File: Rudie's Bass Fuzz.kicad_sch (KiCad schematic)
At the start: 15 parts, among them J1 Conn_01x01_Male, J2 Conn_01x01_Male, J3 Conn_01x01_Male, J4 Conn_01x01_Male, Q1 BC549

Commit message: added led to pcb design
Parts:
- D2: footprint (none) -> LED_THT:LED_D5.0mm
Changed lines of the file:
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@@
     (property "Reference" "D2" (id 0) (at 89.8525 43.18 0))
     (property "Value" "LED" (id 1) (at 89.8525 45.72 0))
-    (property "Footprint" "" (id 2) (at 88.265 50.165 0)
+    (property "Footprint" "LED_THT:LED_D5.0mm" (id 2) (at 88.265 50.165 0)
       (effects (font (size 1.27 1.27)) hide)
     )
@@
     )
     (path "/9bac20ab-0eff-4b4e-96fd-8a8eb787d966"
-      (reference "D2") (unit 1) (value "LED") (footprint "")
+      (reference "D2") (unit 1) (value "LED") (footprint "LED_THT:LED_D5.0mm")
     )
     (path "/0309e1ab-0658-4dbf-89ab-e051ee8674ac"

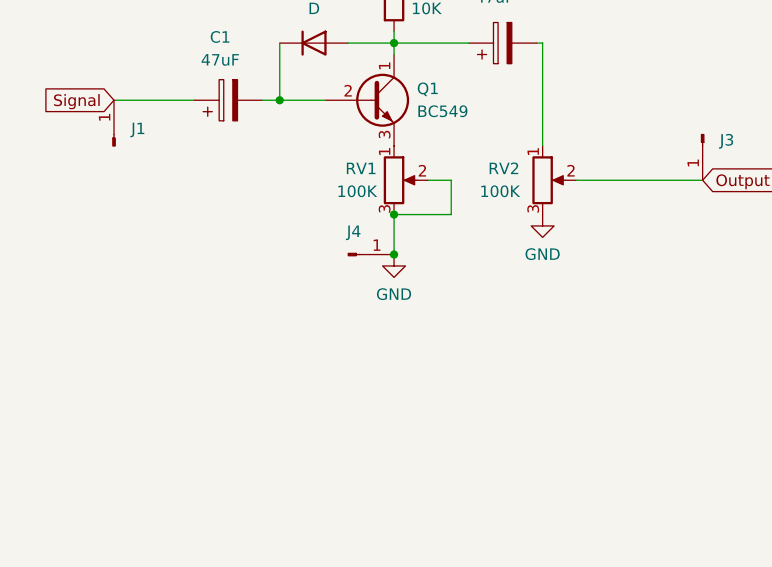
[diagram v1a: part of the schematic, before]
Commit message: removed wires and added extra gnd pins
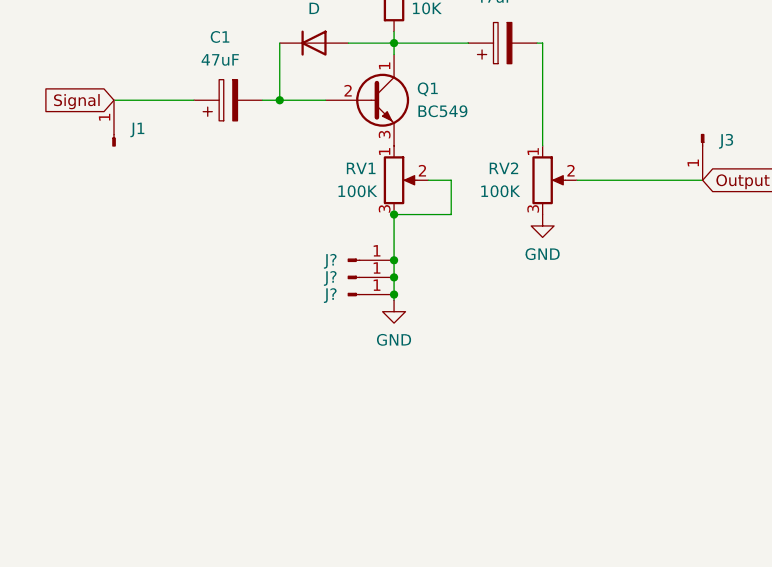
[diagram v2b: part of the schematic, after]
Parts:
- removed J4: Conn_01x01_Male, Connector_Pin:Pin_D1.4mm_L8.5mm_W2.8mm_FlatFork, symbol Connector:Conn_01x01_Male
- added J? (x3): Conn_01x01_Male, Connector_Pin:Pin_D1.4mm_L8.5mm_W2.8mm_FlatFork, symbol Connector:Conn_01x01_Male
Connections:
- net GND: now also J?.1 (Pin_1), J?.1 (Pin_1), J?.1 (Pin_1)
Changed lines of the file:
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@@
   (junction (at 107.315 83.82) (diameter 0) (color 0 0 0 0)
   )
-  (junction (at 107.315 88.265) (diameter 0) (color 0 0 0 0)
-  )
   (junction (at 94.615 71.12) (diameter 0) (color 0 0 0 0)
   )
+  (junction (at 107.315 90.805) (diameter 0) (color 0 0 0 0)
+  )
+  (junction (at 107.315 92.71) (diameter 0) (color 0 0 0 0)
+  )
+  (junction (at 107.315 88.9) (diameter 0) (color 0 0 0 0)
+  )
   (junction (at 84.455 40.64) (diameter 0) (color 0 0 0 0)
   )
@@
     (stroke (width 0) (type default) (color 0 0 0 0))
   )
+  (wire (pts (xy 107.315 88.9) (xy 107.315 90.805))
+    (stroke (width 0) (type default) (color 0 0 0 0))
+  )
+  (wire (pts (xy 107.315 92.71) (xy 107.315 93.345))
+    (stroke (width 0) (type default) (color 0 0 0 0))
+  )
   (wire (pts (xy 84.455 40.64) (xy 107.315 40.64))
     (stroke (width 0) (type default) (color 0 0 0 0))
@@
     (stroke (width 0) (type default) (color 0 0 0 0))
   )
-  (wire (pts (xy 107.315 88.265) (xy 107.315 83.82))
-    (stroke (width 0) (type default) (color 0 0 0 0))
-  )
   (wire (pts (xy 107.315 64.77) (xy 107.315 66.04))
     (stroke (width 0) (type default) (color 0 0 0 0))
@@
     (stroke (width 0) (type default) (color 0 0 0 0))
   )
+  (wire (pts (xy 107.315 83.82) (xy 107.315 88.9))
+    (stroke (width 0) (type default) (color 0 0 0 0))
+  )
   (wire (pts (xy 84.455 40.64) (xy 84.455 50.165))
     (stroke (width 0) (type default) (color 0 0 0 0))
@@
   )
   (wire (pts (xy 127.635 80.01) (xy 141.605 80.01))
+    (stroke (width 0) (type default) (color 0 0 0 0))
+  )
+  (wire (pts (xy 107.315 90.805) (xy 107.315 92.71))
     (stroke (width 0) (type default) (color 0 0 0 0))
   )
@@
     (pin "1")
   )
-  (symbol (lib_id "power:GND") (at 107.315 88.265 0) (unit 1)
-    (in_bom yes) (on_board yes) (fields_autoplaced)
-    (property "Reference" "#PWR01" (id 0) (at 107.315 94.615 0)
-      (effects (font (size 1.27 1.27)) hide)
-    )
-    (property "Value" "GND" (id 1) (at 107.315 92.71 0))
-    (property "Footprint" "" (id 2) (at 107.315 88.265 0)
-      (effects (font (size 1.27 1.27)) hide)
-    )
-    (property "Datasheet" "" (id 3) (at 107.315 88.265 0)
+  (symbol (lib_id "power:GND") (at 107.315 93.345 0) (unit 1)
+    (in_bom yes) (on_board yes) (fields_autoplaced)
+    (property "Reference" "#PWR01" (id 0) (at 107.315 99.695 0)
+      (effects (font (size 1.27 1.27)) hide)
+    )
+    (property "Value" "GND" (id 1) (at 107.315 97.79 0))
+    (property "Footprint" "" (id 2) (at 107.315 93.345 0)
+      (effects (font (size 1.27 1.27)) hide)
+    )
+    (property "Datasheet" "" (id 3) (at 107.315 93.345 0)
       (effects (font (size 1.27 1.27)) hide)
     )
@@
     )
     (property "Datasheet" "~" (id 3) (at 141.605 74.93 0)
-      (effects (font (size 1.27 1.27)) hide)
-    )
-    (pin "1")
-  )
-  (symbol (lib_id "Connector:Conn_01x01_Male") (at 102.235 88.265 0) (unit 1)
-    (in_bom yes) (on_board yes) (fields_autoplaced)
-    (property "Reference" "J4" (id 0) (at 102.87 85.725 0))
-    (property "Value" "Conn_01x01_Male" (id 1) (at 104.1399 86.995 90)
-      (effects (font (size 1.27 1.27)) (justify left) hide)
-    )
-    (property "Footprint" "Connector_Pin:Pin_D1.4mm_L8.5mm_W2.8mm_FlatFork" (id 2) (at 102.235 88.265 0)
-      (effects (font (size 1.27 1.27)) hide)
-    )
-    (property "Datasheet" "~" (id 3) (at 102.235 88.265 0)
       (effects (font (size 1.27 1.27)) hide)
     )
@@
     (pin "2")
   )
+  (symbol (lib_id "Connector:Conn_01x01_Male") (at 102.235 92.71 0) (unit 1)
+    (in_bom yes) (on_board yes)
+    (property "Reference" "J?" (id 0) (at 100.33 92.71 0))
+    (property "Value" "Conn_01x01_Male" (id 1) (at 104.1399 91.44 90)
+      (effects (font (size 1.27 1.27)) (justify left) hide)
+    )
+    (property "Footprint" "Connector_Pin:Pin_D1.4mm_L8.5mm_W2.8mm_FlatFork" (id 2) (at 102.235 92.71 0)
+      (effects (font (size 1.27 1.27)) hide)
+    )
+    (property "Datasheet" "~" (id 3) (at 102.235 92.71 0)
+      (effects (font (size 1.27 1.27)) hide)
+    )
+    (pin "1")
+  )
   (symbol (lib_id "Device:C_Polarized") (at 88.9 71.12 90) (unit 1)
     (in_bom yes) (on_board yes)
@@
     (pin "1")
   )
+  (symbol (lib_id "Connector:Conn_01x01_Male") (at 102.235 90.805 0) (unit 1)
+    (in_bom yes) (on_board yes)
+    (property "Reference" "J?" (id 0) (at 100.33 90.805 0))
+    (property "Value" "Conn_01x01_Male" (id 1) (at 104.1399 89.535 90)
+      (effects (font (size 1.27 1.27)) (justify left) hide)
+    )
+    (property "Footprint" "Connector_Pin:Pin_D1.4mm_L8.5mm_W2.8mm_FlatFork" (id 2) (at 102.235 90.805 0)
+      (effects (font (size 1.27 1.27)) hide)
+    )
+    (property "Datasheet" "~" (id 3) (at 102.235 90.805 0)
+      (effects (font (size 1.27 1.27)) hide)
+    )
+    (pin "1")
+  )
+  (symbol (lib_id "Connector:Conn_01x01_Male") (at 102.235 88.9 0) (unit 1)
+    (in_bom yes) (on_board yes)
+    (property "Reference" "J?" (id 0) (at 100.33 88.9 0))
+    (property "Value" "Conn_01x01_Male" (id 1) (at 104.1399 87.63 90)
+      (effects (font (size 1.27 1.27)) (justify left) hide)
+    )
+    (property "Footprint" "Connector_Pin:Pin_D1.4mm_L8.5mm_W2.8mm_FlatFork" (id 2) (at 102.235 88.9 0)
+      (effects (font (size 1.27 1.27)) hide)
+    )
+    (property "Datasheet" "~" (id 3) (at 102.235 88.9 0)
+      (effects (font (size 1.27 1.27)) hide)
+    )
+    (pin "1")
+  )
   (sheet_instances
     (path "/" (page "1"))
@@
       (reference "J3") (unit 1) (value "Conn_01x01_Male") (footprint "Connector_Pin:Pin_D1.4mm_L8.5mm_W2.8mm_FlatFork")
     )
-    (path "/7a1a31a1-be13-4299-817f-015138e93643"
-      (reference "J4") (unit 1) (value "Conn_01x01_Male") (footprint "Connector_Pin:Pin_D1.4mm_L8.5mm_W2.8mm_FlatFork")
+    (path "/84696f8a-20a3-40b7-aedb-09285a52328e"
+      (reference "J?") (unit 1) (value "Conn_01x01_Male") (footprint "Connector_Pin:Pin_D1.4mm_L8.5mm_W2.8mm_FlatFork")
+    )
+    (path "/e27eb912-b00a-4827-9110-e3585acda442"
+      (reference "J?") (unit 1) (value "Conn_01x01_Male") (footprint "Connector_Pin:Pin_D1.4mm_L8.5mm_W2.8mm_FlatFork")
+    )
+    (path "/ed80c364-dffb-4bce-83fe-922f0e755acb"
+      (reference "J?") (unit 1) (value "Conn_01x01_Male") (footprint "Connector_Pin:Pin_D1.4mm_L8.5mm_W2.8mm_FlatFork")
     )
     (path "/ac98c4da-cede-4def-8a6f-fc1401ef6f5d"

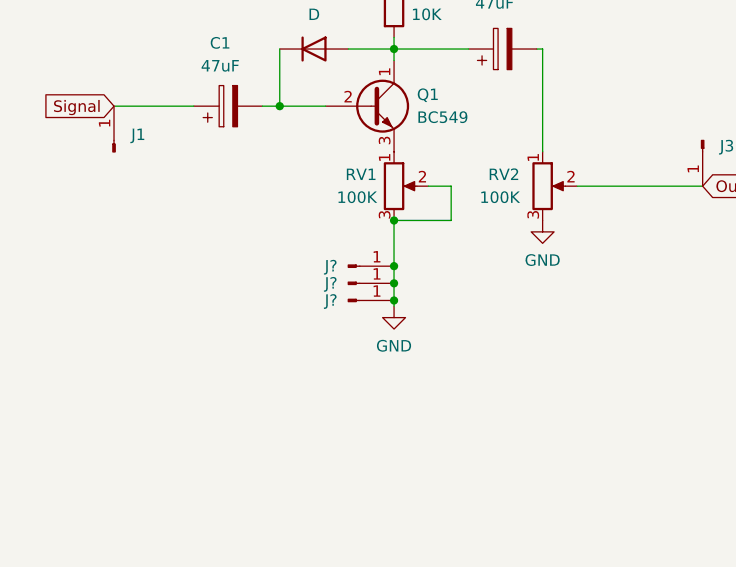
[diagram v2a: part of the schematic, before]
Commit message: silkscreen cleanup
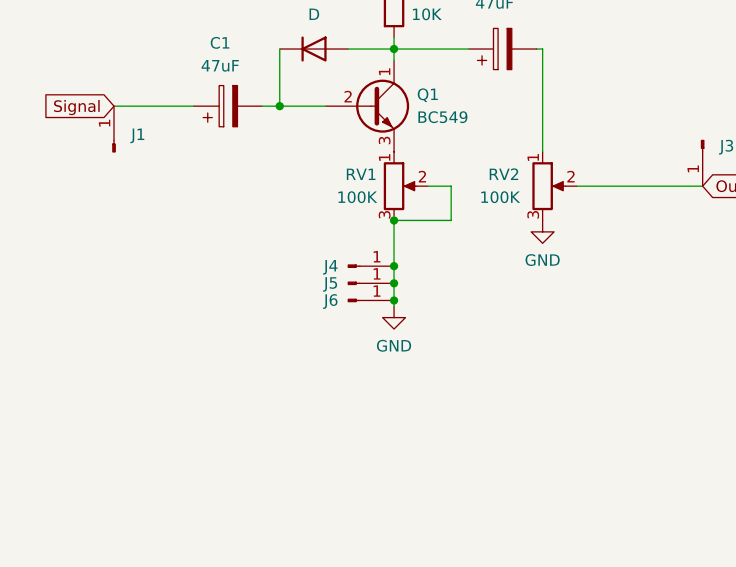
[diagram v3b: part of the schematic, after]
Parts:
- gave numbers to parts that had none: 3
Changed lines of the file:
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@@
   (symbol (lib_id "Connector:Conn_01x01_Male") (at 102.235 92.71 0) (unit 1)
     (in_bom yes) (on_board yes)
-    (property "Reference" "J?" (id 0) (at 100.33 92.71 0))
+    (property "Reference" "J6" (id 0) (at 100.33 92.71 0))
     (property "Value" "Conn_01x01_Male" (id 1) (at 104.1399 91.44 90)
       (effects (font (size 1.27 1.27)) (justify left) hide)
@@
   (symbol (lib_id "Connector:Conn_01x01_Male") (at 102.235 90.805 0) (unit 1)
     (in_bom yes) (on_board yes)
-    (property "Reference" "J?" (id 0) (at 100.33 90.805 0))
+    (property "Reference" "J5" (id 0) (at 100.33 90.805 0))
     (property "Value" "Conn_01x01_Male" (id 1) (at 104.1399 89.535 90)
       (effects (font (size 1.27 1.27)) (justify left) hide)
@@
   (symbol (lib_id "Connector:Conn_01x01_Male") (at 102.235 88.9 0) (unit 1)
     (in_bom yes) (on_board yes)
-    (property "Reference" "J?" (id 0) (at 100.33 88.9 0))
+    (property "Reference" "J4" (id 0) (at 100.33 88.9 0))
     (property "Value" "Conn_01x01_Male" (id 1) (at 104.1399 87.63 90)
       (effects (font (size 1.27 1.27)) (justify left) hide)
@@
       (reference "J3") (unit 1) (value "Conn_01x01_Male") (footprint "Connector_Pin:Pin_D1.4mm_L8.5mm_W2.8mm_FlatFork")
     )
+    (path "/ed80c364-dffb-4bce-83fe-922f0e755acb"
+      (reference "J4") (unit 1) (value "Conn_01x01_Male") (footprint "Connector_Pin:Pin_D1.4mm_L8.5mm_W2.8mm_FlatFork")
+    )
+    (path "/e27eb912-b00a-4827-9110-e3585acda442"
+      (reference "J5") (unit 1) (value "Conn_01x01_Male") (footprint "Connector_Pin:Pin_D1.4mm_L8.5mm_W2.8mm_FlatFork")
+    )
     (path "/84696f8a-20a3-40b7-aedb-09285a52328e"
-      (reference "J?") (unit 1) (value "Conn_01x01_Male") (footprint "Connector_Pin:Pin_D1.4mm_L8.5mm_W2.8mm_FlatFork")
-    )
-    (path "/e27eb912-b00a-4827-9110-e3585acda442"
-      (reference "J?") (unit 1) (value "Conn_01x01_Male") (footprint "Connector_Pin:Pin_D1.4mm_L8.5mm_W2.8mm_FlatFork")
-    )
-    (path "/ed80c364-dffb-4bce-83fe-922f0e755acb"
-      (reference "J?") (unit 1) (value "Conn_01x01_Male") (footprint "Connector_Pin:Pin_D1.4mm_L8.5mm_W2.8mm_FlatFork")
+      (reference "J6") (unit 1) (value "Conn_01x01_Male") (footprint "Connector_Pin:Pin_D1.4mm_L8.5mm_W2.8mm_FlatFork")
     )
     (path "/ac98c4da-cede-4def-8a6f-fc1401ef6f5d"
